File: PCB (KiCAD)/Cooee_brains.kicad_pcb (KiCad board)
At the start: 2 copper layers, 66.8 x 48.7 mm, 26 parts, among them J1 USB4105-GF-A, J4 Conn_01x14_Socket, J5 Conn_02x20_Counter_Clockwise, SW1 Prog, SW2 Reset, U1 AMS1117-3.3, U2 ESP32-S3-WROOM-1-N8, U3 SX1262IMLTRT, U4 RXM-GPS-FM

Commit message: motherboard PCB layout work
motherboard PCB layout work
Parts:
- removed J5: Conn_02x20_Counter_Clockwise, Connector_PinHeader_2.54mm:PinHeader_2x20_P2.54mm_Vertical_SMD
- added J2: Conn_Coaxial, Connector_Coaxial:U.FL_Molex_MCRF_73412-0110_Vertical, B.Cu at (139.3, 86.9)
- added J3: 503398-1892, USB4105-GF-A (1):MOLEX_503398-1892, B.Cu at (180.0, 124.0)
- added J6: Conn_Coaxial, Connector_Coaxial:U.FL_Molex_MCRF_73412-0110_Vertical, B.Cu at (189.4, 92.9)
- added J7: Conn_01x04_Pin, Connector_PinHeader_2.54mm:PinHeader_1x04_P2.54mm_Horizontal, B.Cu at (183.0, 83.7)
- added J9: Conn_01x18_Socket, Connector_PinSocket_2.54mm:PinSocket_1x18_P2.54mm_Vertical_SMD_Pin1Left, F.Cu at (167.0, 117.9)
- added MK1: INMP441, USB4105-GF-A (1):MIC_INMP441, B.Cu at (169.7, 128.3)
- added U5: ~, USB4105-GF-A (1):M210Z, B.Cu at (179.4, 96.4)
- J4: footprint Connector_PinSocket_2.54mm:PinSocket_1x14_P2.54mm_Vertical -> Connector_PinSocket_2.54mm:PinSocket_1x14_P2.54mm_Horizontal
- U3: value SX1262IMLTRT -> MAX98357AETE_T
- U4: value RXM-GPS-FM -> SX1262IMLTRT; footprint RF_GPS:Linx_RXM-GPS -> Package_DFN_QFN:QFN-24-1EP_4x4mm_P0.5mm_EP2.6x2.6mm
- moved U4 53.9 mm to (133.0, 100.3), turned to 0 degrees
- moved U3 21.0 mm to (142.1, 100.0)
- moved J4 4.10 mm to (176.9, 91.3)
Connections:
- net OLED_CLK renamed T_CS
- net OLED_DIN renamed T_DIN
- net OLED_RST renamed Display_LED
- J4 pad 1: unconnected-(J4-Pin_1-Pad1) -> Display_VCC
- J4 pad 10: OLED_CS -> T_CLK
- J4 pad 13: GND -> T_DO
- J4 pad 14: 3.3V -> T_TRO
- J4 pad 2: unconnected-(J4-Pin_2-Pad2) -> GND
- J4 pad 3: unconnected-(J4-Pin_3-Pad3) -> Display_CS
- J4 pad 4: unconnected-(J4-Pin_4-Pad4) -> Display_RST
- J4 pad 5: unconnected-(J4-Pin_5-Pad5) -> Display_DC
- J4 pad 6: unconnected-(J4-Pin_6-Pad6) -> Display_MOSI
- J4 pad 7: unconnected-(J4-Pin_7-Pad7) -> Display_SCK
- J4 pad 9: OLED_DC -> Display_MISO
- U2 pad 24: OLED_CS -> unconnected-(U2-IO47-Pad24)
- U2 pad 25: OLED_DC -> unconnected-(U2-IO48-Pad25)
- U3 pad 10: unconnected-(U3-VBAT-Pad10) -> SPEAKER+
- U3 pad 11: unconnected-(U3-VBAT_IO-Pad11) -> GND
- U3 pad 12: unconnected-(U3-DIO2-Pad12) -> (no net)
- U3 pad 13: unconnected-(U3-DIO1-Pad13) -> (no net)
- U3 pad 15: unconnected-(U3-~{RESET}-Pad15) -> GND
- U3 pad 18: unconnected-(U3-SCK-Pad18) -> (no net)
- U3 pad 19: unconnected-(U3-NSS-Pad19) -> (no net)
- U3 pad 2: GND -> unconnected-(U3-GAIN_SLOT-Pad2)
- U3 pad 20: GND -> (no net)
- U3 pad 21: unconnected-(U3-RFI_P-Pad21) -> (no net)
- U3 pad 22: unconnected-(U3-RFI_N-Pad22) -> (no net)
- U3 pad 23: unconnected-(U3-RFO-Pad23) -> (no net)
- U3 pad 24: unconnected-(U3-VR_PA-Pad24) -> (no net)
- U3 pad 25: GND -> (no net)
- U3 pad 3: unconnected-(U3-XTA-Pad3) -> GND
- U3 pad 5: GND -> (no net)
- U3 pad 6: unconnected-(U3-DIO3-Pad6) -> (no net)
- U3 pad 7: unconnected-(U3-VREG-Pad7) -> VDD
- U3 pad 8: GND -> VDD
- U3 pad 9: unconnected-(U3-DCC_SW-Pad9) -> SPEAKER-
- U4 pad 17: (no net) -> unconnected-(U4-MOSI-Pad17)
- U4 pad 18: GND -> unconnected-(U4-SCK-Pad18)
- U4 pad 2: unconnected-(U4-NC-Pad2) -> GND
- U4 pad 21: GND -> unconnected-(U4-RFI_P-Pad21)
- U4 pad 22: GND -> unconnected-(U4-RFI_N-Pad22)
- U4 pad 5: unconnected-(U4-RX-Pad5) -> GND
- U4 pad 8: unconnected-(U4-~{RESET}-Pad8) -> GND
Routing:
- net Net-(J6-In): track 0.00 -> 6.69 mm
- net ROW2: track 5.05 -> 0.00 mm
- net COL7: track 5.05 -> 0.00 mm
- net COL4: track 5.05 -> 0.00 mm
- net ROW5: track 5.05 -> 0.00 mm
- net ROW4: track 5.05 -> 0.00 mm
- net ROW3: track 5.05 -> 0.00 mm
- net ROW1: track 5.05 -> 0.00 mm
- net COL9: track 5.05 -> 0.00 mm
- net COL8: track 5.05 -> 0.00 mm
- net COL6: track 5.05 -> 0.00 mm
- net COL5: track 5.05 -> 0.00 mm
- net COL3: track 5.05 -> 0.00 mm
- net COL2: track 5.05 -> 0.00 mm
- net COL10: track 5.05 -> 0.00 mm
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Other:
- board size 66.8 x 48.7 mm -> 66.8 x 60.5 mm
- board text added: "SCK"

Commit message: swapped out complex SX1262 circuitry for a module
swapped out complex SX1262 circuitry for a module
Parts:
- removed U4: SX1262IMLTRT, Package_DFN_QFN:QFN-24-1EP_4x4mm_P0.5mm_EP2.6x2.6mm
- added U6: INTERFACE-CP2102-GMR_QFN28_, USB4105-GF-A (1):QFN28G_0.5-5X5MM, B.Cu at (133.6, 95.9)
- added U8: RA-01H, RF_Module:Ai-Thinker-Ra-01-LoRa, B.Cu at (182.4, 99.8)
- moved J2 44.5 mm to (176.6, 111.3)
- moved J6 21.1 mm to (168.3, 92.3)
- moved U5 20.0 mm to (159.4, 96.4)
- moved J4 4.08 mm to (176.9, 87.2)
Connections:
- J2 pad 1: unconnected-(J2-In-Pad1) -> Net-(J2-In)
- J2 pad 2: unconnected-(J2-Ext-Pad2) -> GND
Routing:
- net Net-(J2-In): track 0.00 -> 3.91 mm
- net GND: track 4.79 -> 7.81 mm
- net BigSD_SCK: track 2.10 -> 0.00 mm
- net Net-(J6-In): track 6.69 -> 5.26 mm
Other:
- board size 66.8 x 60.5 mm -> 66.8 x 51 mm
- board text added: "GPS"

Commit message: more PCB work
should have the 90 degree SMD header pins lined up to mount now, unfortunately I've invalidated the keyboard prototypes I already bought
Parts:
- moved J9 10.3 mm to (157.0, 120.2), turned to 90 degrees

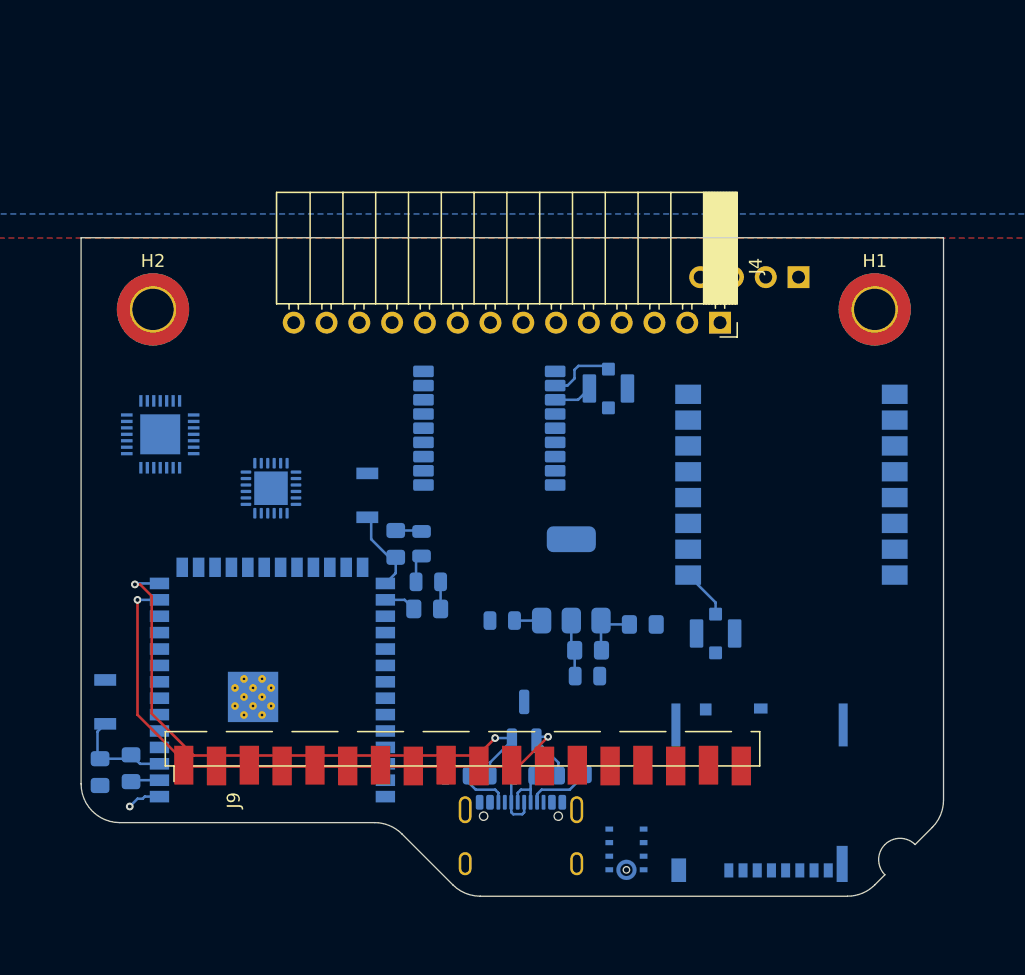
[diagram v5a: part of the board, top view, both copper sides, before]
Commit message: finalized next prototype of keyboard PCB, ready to order
finalized next prototype of keyboard PCB, ready to order
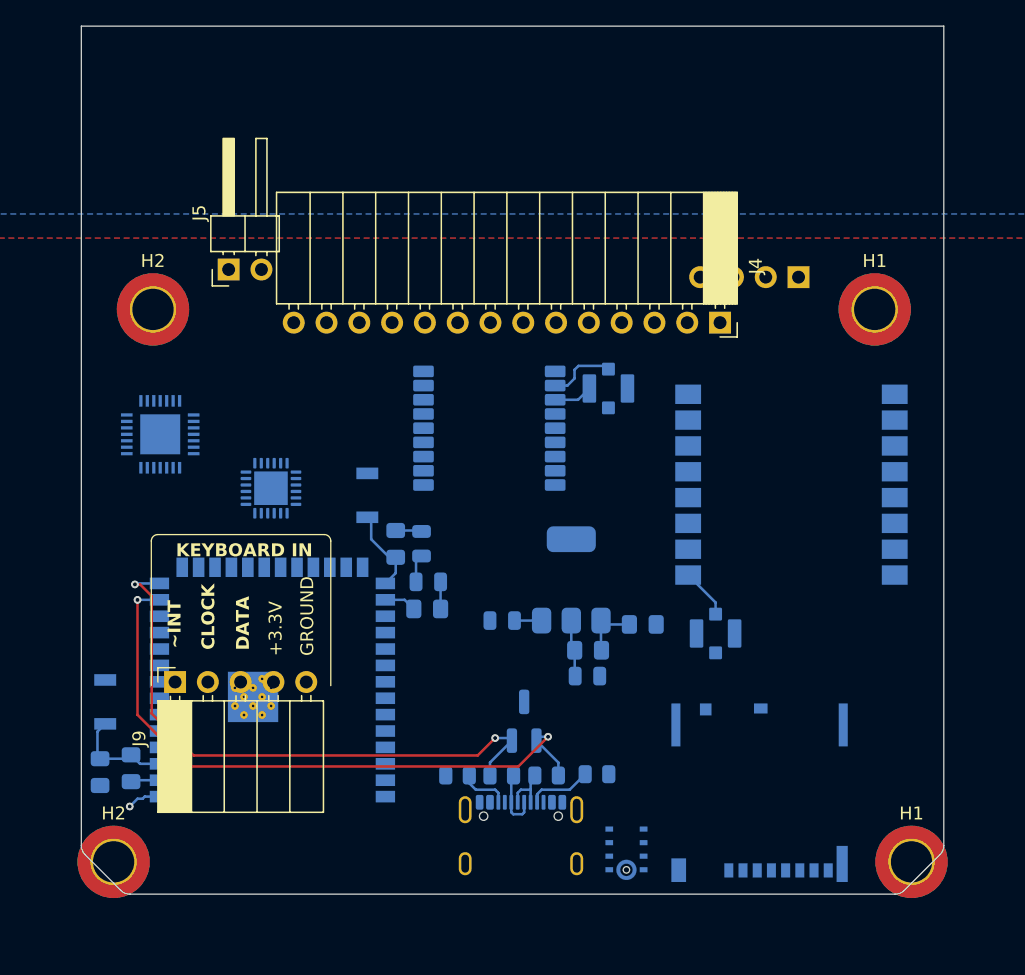
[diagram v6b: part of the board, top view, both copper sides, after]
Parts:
- added H1: MountingHole_Pad, MountingHole:MountingHole_3.2mm_M3_DIN965_Pad_TopBottom, F.Cu at (191.8, 129.0)
- added H2: MountingHole_Pad, MountingHole:MountingHole_3.2mm_M3_DIN965_Pad_TopBottom, F.Cu at (129.9, 129.0)
- added J5: Conn_01x02_Pin, Connector_PinHeader_2.54mm:PinHeader_1x02_P2.54mm_Horizontal, F.Cu at (138.9, 83.1)
- J9: value Conn_01x18_Socket -> Conn_01x05_Socket; footprint Connector_PinSocket_2.54mm:PinSocket_1x18_P2.54mm_Vertical_SMD_Pin1Left -> Connector_PinSocket_2.54mm:PinSocket_1x05_P2.54mm_Horizontal
- moved J9 22.9 mm to (134.7, 115.1)
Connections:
- J4 pad 1: Display_VCC -> 3.3V
- J4 pad 12: T_DIN -> T_MOSI
- J4 pad 13: T_DO -> T_MISO
- J4 pad 14: T_TRO -> T_IRQ
- J4 pad 8: Display_LED -> Display_LED_BacklightEN
- J9 pad 1: GND -> KEEP_RST
- J9 pad 2: +3.3V -> KEEB_SCL
- J9 pad 3: COL1 -> KEEB_D
- J9 pad 4: ROW1 -> 3.3V
- J9 pad 5: COL7 -> GND
- U2 pad 12: unconnected-(U2-IO8-Pad12) -> Display_MOSI
- U2 pad 15: unconnected-(U2-IO3-Pad15) -> KEEB_SCL
- U2 pad 16: unconnected-(U2-IO46-Pad16) -> LoRa_Select
- U2 pad 17: unconnected-(U2-IO9-Pad17) -> Display_SCK
- U2 pad 18: unconnected-(U2-IO10-Pad18) -> Display_LED_BacklightEN
- U2 pad 19: unconnected-(U2-IO11-Pad19) -> Display_MISO
- U2 pad 20: unconnected-(U2-IO12-Pad20) -> T_CLK
- U2 pad 21: unconnected-(U2-IO13-Pad21) -> T_CS
- U2 pad 22: unconnected-(U2-IO14-Pad22) -> T_MOSI
- U2 pad 24: unconnected-(U2-IO47-Pad24) -> LoRa_MOSI
- U2 pad 25: unconnected-(U2-IO48-Pad25) -> LoRa_MISO
- U2 pad 26: unconnected-(U2-IO45-Pad26) -> LoRa_SCLK
- U2 pad 29: unconnected-(U2-IO36-Pad29) -> SHARED_MOSI
- U2 pad 30: unconnected-(U2-IO37-Pad30) -> SHARED_MISO
- U2 pad 31: unconnected-(U2-IO38-Pad31) -> SHARED_CLCK
- U2 pad 38: unconnected-(U2-IO2-Pad38) -> KEEP_RST
- U2 pad 4: unconnected-(U2-IO4-Pad4) -> KEEB_D
- U2 pad 5: unconnected-(U2-IO5-Pad5) -> Display_CS
- U2 pad 6: unconnected-(U2-IO6-Pad6) -> Display_RST
- U2 pad 7: unconnected-(U2-IO7-Pad7) -> Display_DC
- U2 pad 8: unconnected-(U2-IO15-Pad8) -> T_MISO
- U2 pad 9: unconnected-(U2-IO16-Pad9) -> T_IRQ
- U6 pad 29: unconnected-(U6-GND@1-Pad29) -> GND
- U6 pad 3: unconnected-(U6-GND-Pad3) -> GND
- U6 pad 4: unconnected-(U6-D+-Pad4) -> USB_D+
- U6 pad 5: unconnected-(U6-D--Pad5) -> USB_D-
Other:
- board size 66.8 x 51 mm -> 66.8 x 67.2 mm
- board text added: "+3.3V"
- board text added: "CLOCK"
- board text added: "DATA"
- board text added: "GROUND"
- board text added: "KEYBOARD IN"
- board text added: "~INT"

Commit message: pcb layout work on phone motherboard
pcb layout work on phone motherboard
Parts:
- added Keyboard1: Keyboard, TestPoint:TestPoint_Pad_1.0x1.0mm, F.Cu at (129.9, 129.0)
- H1, H2: value MountingHole_Pad -> MountingHole_Pad_MP
- moved H1 1.00 mm to (187.9, 86.2)
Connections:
- H1 pad 1: GND -> (no net)
- H2 pad 1: GND -> (no net)
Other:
- board size 66.8 x 67.2 mm -> 66.8 x 150.6 mm

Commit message: more PCB work on the motherboard
more PCB work on the motherboard
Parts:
- added C5: 4.7uF, Capacitor_SMD:C_0805_2012Metric, B.Cu at (258.0, 82.8)
- added C6: 100nF, Capacitor_SMD:C_0805_2012Metric, B.Cu at (262.1, 73.1)
- added C7: 1uF, Capacitor_SMD:C_0805_2012Metric, B.Cu at (262.1, 75.2)
- added C8: 100nF, Capacitor_SMD:C_0805_2012Metric, B.Cu at (262.1, 71.0)
- added C9: 4.7uF, Capacitor_SMD:C_0805_2012Metric, B.Cu at (258.1, 71.0)
- added D1: D, Diode_SMD:D_0805_2012Metric_Pad1.15x1.40mm_HandSolder, F.Cu at (225.4, 24.2)
- added H3: MountingHole_Pad_MP, MountingHole:MountingHole_3.2mm_M3_DIN965_Pad_TopBottom, F.Cu at (133.2, -15.9)
- added R11: 10kΩ, Capacitor_SMD:C_0805_2012Metric_Pad1.18x1.45mm_HandSolder, B.Cu at (263.8, 77.3)
- added R12: 10kΩ, Capacitor_SMD:C_0805_2012Metric_Pad1.18x1.45mm_HandSolder, F.Cu at (220.6, 24.2)
- added R13: 10kΩ, Capacitor_SMD:C_0805_2012Metric_Pad1.18x1.45mm_HandSolder, F.Cu at (220.6, 27.2)
- added R14: 10kΩ, Capacitor_SMD:C_0805_2012Metric_Pad1.18x1.45mm_HandSolder, F.Cu at (220.6, 30.2)
- added R8: 10kΩ, Capacitor_SMD:C_0805_2012Metric_Pad1.18x1.45mm_HandSolder, B.Cu at (262.9, 79.6)
- U5: value ~ -> M210Z
- moved U6 124.8 mm to (257.0, 78.0), turned to -90 degrees
- moved C3 99.5 mm to (245.0, 64.5)
- moved C4 99.5 mm to (220.1, 82.2)
- moved D74 99.5 mm to (245.5, 67.5)
- moved R1 99.5 mm to (245.4, 69.6)
- moved R10 99.5 mm to (222.5, 81.9)
- moved R9 99.5 mm to (243.0, 64.5)
- moved SW1 99.5 mm to (240.8, 60.8)
- moved SW2 99.5 mm to (220.5, 76.8)
- moved U2 99.5 mm to (233.4, 78.9)
- moved MK1 40.0 mm to (130.6, 119.9)
- moved U3 5.93 mm to (140.0, 94.5)
- moved J4 0.19 mm to (177.1, 87.2)
- moved H1 0.19 mm to (188.1, 86.2)
- moved H2 0.19 mm to (133.2, 86.2)
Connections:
- net KEEP_RST renamed KEEB_INT
- C1 pad 2: 5V -> Batt+
- J3 pad 2: unconnected-(J3-CD/DAT3^2-Pad2) -> MICRO_SD_CS
- J3 pad 3: unconnected-(J3-CMD-Pad3) -> SHARED_MOSI
- J3 pad 4: unconnected-(J3-VDD-Pad4) -> 3.3V
- J3 pad 5: SD_CLK -> SHARED_CLCK
- J3 pad 7: SD_DAT0 -> SHARED_MISO
- J4 pad 10: T_CLK -> SHARED_CLCK
- J4 pad 12: T_MOSI -> SHARED_MOSI
- J4 pad 13: T_MISO -> SHARED_MISO
- J5 pad 1: SPEAKER+ -> SPEAKER-
- J5 pad 2: SPEAKER- -> SPEAKER+
- J7 pad 1: BigSD_SCK -> SHARED_CLCK
- J7 pad 2: BigSD_MISO -> SHARED_MISO
- J7 pad 3: BigSD_MOSI -> SHARED_MOSI
- MK1 pad 1: unconnected-(MK1-SCK-Pad1) -> MIC_BCLK
- MK1 pad 2: unconnected-(MK1-SD-Pad2) -> MIC_DOUT
- MK1 pad 3: unconnected-(MK1-WS-Pad3) -> MIC_LRCK
- MK1 pad 4: unconnected-(MK1-L/R-Pad4) -> Net-(MK1-L/R)
- MK1 pad 7: unconnected-(MK1-VDD-Pad7) -> 3.3V
- MK1 pad 8: unconnected-(MK1-CHIPEN-Pad8) -> MIC_EN
- U1 pad 3: 5V -> Batt+
- U2 pad 10: unconnected-(U2-IO17-Pad10) -> KEEB_SCL
- U2 pad 11: unconnected-(U2-IO18-Pad11) -> MIC_BCLK
- U2 pad 13: USB_DN -> MIC_LRCK
- U2 pad 14: USB_DP -> MIC_DOUT
- U2 pad 15: KEEB_SCL -> unconnected-(U2-IO3-Pad15)
- U2 pad 16: LoRa_Select -> unconnected-(U2-IO46-Pad16)
- U2 pad 20: T_CLK -> SPKR_BCLK
- U2 pad 21: T_CS -> SPKR_DIN
- U2 pad 22: T_MOSI -> SPKR_LRCK
- U2 pad 23: unconnected-(U2-IO21-Pad23) -> MIC_EN
- U2 pad 24: LoRa_MOSI -> unconnected-(U2-IO47-Pad24)
- U2 pad 25: LoRa_MISO -> LoRa_Select
- U2 pad 26: LoRa_SCLK -> unconnected-(U2-IO45-Pad26)
- U2 pad 32: unconnected-(U2-IO39-Pad32) -> GPS_RST
- U2 pad 33: unconnected-(U2-IO40-Pad33) -> GPS_On/OFF
- U2 pad 34: unconnected-(U2-IO41-Pad34) -> GPS_SlaveIn
- U2 pad 35: unconnected-(U2-IO42-Pad35) -> GPS_SlaveOut
- U2 pad 36: unconnected-(U2-RXD0-Pad36) -> Interface_Tx
- U2 pad 37: unconnected-(U2-TXD0-Pad37) -> Interface_Rx
- U2 pad 8: T_MISO -> T_CS
- U3 pad 1: unconnected-(U3-DIN-Pad1) -> SPKR_DIN
- U3 pad 14: unconnected-(U3-LRCLK-Pad14) -> SPKR_LRCK
- U3 pad 16: unconnected-(U3-BCLK-Pad16) -> SPKR_BCLK
- U3 pad 17: unconnected-(U3-EP-Pad17) -> SPKR_EN
- U3 pad 2: unconnected-(U3-GAIN_SLOT-Pad2) -> Net-(U3-GAIN_SLOT)
- U3 pad 4: unconnected-(U3-SD_MODE-Pad4) -> Net-(U3-SD_MODE)
- U5 pad 14: unconnected-(U5-Vcc_RF-Pad14) -> 3.3V
- U5 pad 2: unconnected-(U5-GPS_TxData-Pad2) -> GPS_SlaveOut
- U5 pad 3: unconnected-(U5-GPS_RxData-Pad3) -> GPS_SlaveIn
- U5 pad 5: unconnected-(U5-On/Off-Pad5) -> GPS_On/OFF
- U5 pad 8: unconnected-(U5-VCC-Pad8) -> 3.3V
- U5 pad 9: unconnected-(U5-RST-Pad9) -> GPS_RST
- U6 pad 11: unconnected-(U6-~{SUSPEND}-Pad11) -> Net-(U6-~{SUSPEND})
- U6 pad 18: unconnected-(U6-NC/VPP-Pad18) -> Net-(U6-NC/VPP)
- U6 pad 25: unconnected-(U6-RXD-Pad25) -> Interface_Rx
- U6 pad 26: unconnected-(U6-TXD-Pad26) -> Interface_Tx
- U6 pad 4: USB_D+ -> USB_DP
- U6 pad 5: USB_D- -> USB_DN
- U6 pad 6: unconnected-(U6-VDD-Pad6) -> 3.3V
- U6 pad 7: unconnected-(U6-REGIN-Pad7) -> 5V
- U6 pad 8: unconnected-(U6-VBUS-Pad8) -> 5V
- U6 pad 9: unconnected-(U6-~{RST}-Pad9) -> Net-(U6-~{RST})
- U8 pad 12: LoRa_SCLK -> SHARED_CLCK
- U8 pad 13: LoRa_MISO -> SHARED_MISO
- U8 pad 14: LoRa_MOSI -> SHARED_MOSI
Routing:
- net USB_DN: track 49.4 -> 3.83 mm, vias 2 -> 0
- net USB_DP: track 46.0 -> 3.69 mm, vias 2 -> 0
- net 3.3V: track 8.65 -> 15.7 mm
- net 5V: track 2.10 -> 9.08 mm
- net Net-(U6-~{SUSPEND}): track 0.00 -> 3.25 mm
- net Net-(U6-~{RST}): track 0.00 -> 3.23 mm
- net Net-(U6-NC/VPP): track 0.00 -> 2.31 mm
- net Batt+: track 0.00 -> 2.10 mm
- net Interface_Rx: track 0.00 -> 1.67 mm
- net Interface_Tx: track 0.00 -> 1.59 mm
- net GND: track 7.81 -> 9.33 mm, vias 1 -> 0
- net EN: track 8.04 -> 7.34 mm
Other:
- board size 66.8 x 150.6 mm -> 66.8 x 151.3 mm
- board text added: "SPACE FOR BATTERY"
- board text added: "SPACE FOR SPEAKER"
